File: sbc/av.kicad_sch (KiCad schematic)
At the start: 4 parts, among them J5 AVD-Header, J6 AVA-Header, J7 AudioOut-Connector, J8 VideoOut-Connector

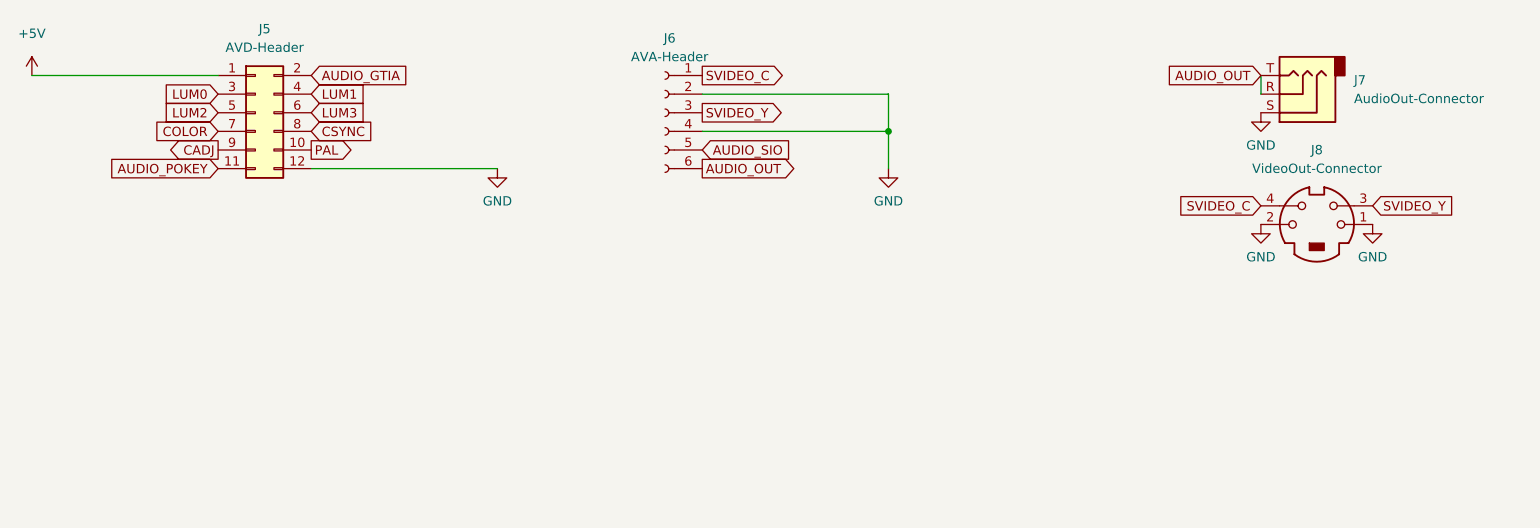
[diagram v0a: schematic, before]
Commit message: SBC v1.1
PCB fixes/changes:

  - Permanently power voltage translators
  - Conservatively specified a slower SRAM (the previous/faster SRAM does actually work fine)
  - RMU: Speculatively provided unbuffered PHI0 input and OE output (not actually needed)
  - Add pullups to open drain GTIA outputs
  - Plot selected values on silk screen
  - Accommodate KiCad 7 upgrade

- PLD changes:
  - Fix AMU logic
  - Fix RMU (unbuffered PHI0 and OE output not needed)

- QTPY firmware:
  - add soft power on/off support (Ctrl-F12)
  - reflects switched power and usb state in the neopixel
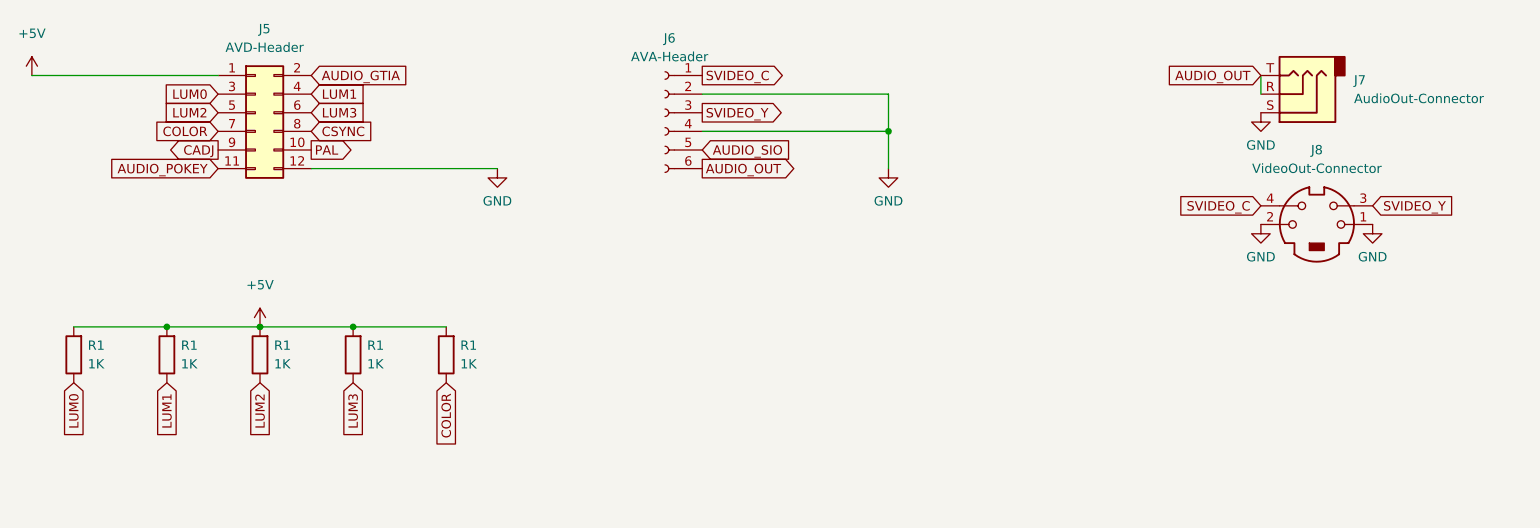
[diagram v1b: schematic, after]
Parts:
- added R1 (x5): 1K, Resistor_SMD:R_0805_2012Metric_Pad1.20x1.40mm_HandSolder, symbol Device:R
- J6: symbol Connector:Conn_01x06_Female -> Connector:Conn_01x06_Socket
- J7: symbol Connector:AudioJack3 -> Connector_Audio:AudioJack3
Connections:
- net +5V: now also R1.2, R1.2, R1.2, R1.2, R1.2
- net COLOR: now also R1.1
- net LUM0: now also R1.1
- net LUM1: now also R1.1
- net LUM2: now also R1.1
- net LUM3: now also R1.1

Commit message: SBC v1.2
SBC fixes/changes:

  - S-Video:
    - Fix S-Video footprint (Y and C swapped, and GNDs swapped) and adapt schematic to match
    - Wire S-Video grounds to AVA header instead of directly to (digital) GND
  - Audio:
    - Wire Audio-Out ground to AVA header
    - Drop SIO audio
    - Pullup open drain pokey audio
  - AMU/RMU:
    - Connect ROM and RAM OE to GND
    - Reserve AMU pin for "IO"
    - Reserve RMU pin for "antic" (registered halt)
    - Support for separate Antic banking (clock RMU with /phi2)
    - Supoprt 130XE and 320XE (compy)
  - Add the option for a resistor between OSC, PHI0 buffer and PHI2 buffer (to reduce over/under-shoot)
  - Invert CA2 (a PNP transistor on the Atari 800 XL inverts this signal)

Additions:

  - SBC Audio/Video board
  - SBC Case
  - SBC SD board

Stylize the complete system as "SFF 320XE".
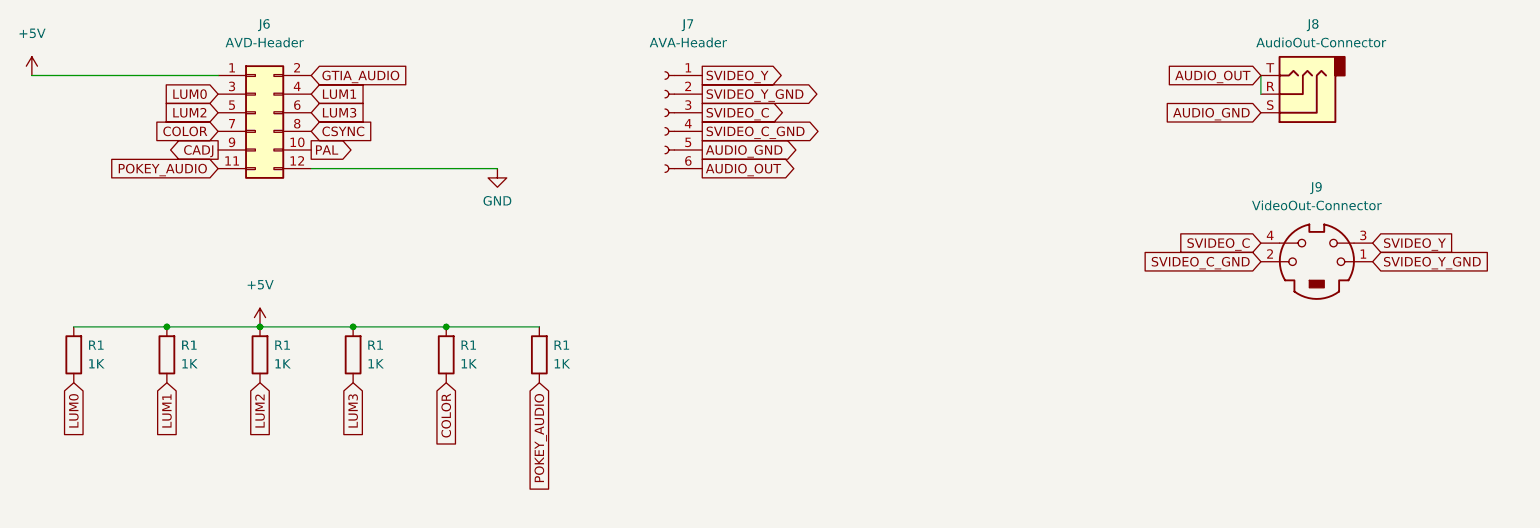
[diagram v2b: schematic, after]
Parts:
- added R1: 1K, Resistor_SMD:R_0805_2012Metric_Pad1.20x1.40mm_HandSolder, symbol Device:R
- renumbered J5 to J6, J6 to J7, J7 to J8, J8 to J9
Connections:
- net +5V: now also R1.2
- net GND: no longer J7.2 (Pin_2), J7.4 (Pin_4), J8.S, J9.1, J9.2
- net SVIDEO_C: now also J7.3 (Pin_3); no longer J7.1 (Pin_1)
- net SVIDEO_Y: now also J7.1 (Pin_1); no longer J7.3 (Pin_3)
- net AUDIO_GTIA renamed GTIA_AUDIO
- net AUDIO_POKEY renamed POKEY_AUDIO
- net POKEY_AUDIO: now also R1.1
- net AUDIO_SIO renamed AUDIO_GND
- net AUDIO_GND: now also J8.S
- new net SVIDEO_C_GND: J7.4 (Pin_4), J9.2
- new net SVIDEO_Y_GND: J7.2 (Pin_2), J9.1
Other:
- moved on the sheet: J9

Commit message: SBC v1.3
Motherboard updates:

  - KiCad 9 upgrade
  - USB-C power connector
  - Replace EOL resistor packs with discrete SMD resistors
  - Power/enable voltage translators from switched 5V
  - Fix motor signal pullup
  - Eliminate loop in phi2 traces
  - Thicker clock signal traces

SD card adapter updates:

  - KiCad 9 upgrade
  - Power/enable voltage translator from switched 5V and the eliminate unnecessary SIO pullups

Audio/Video adapter updates:

  - KiCad 9 upgrade
  - No functional changes, gerbers not regenerated, cleaned up bom
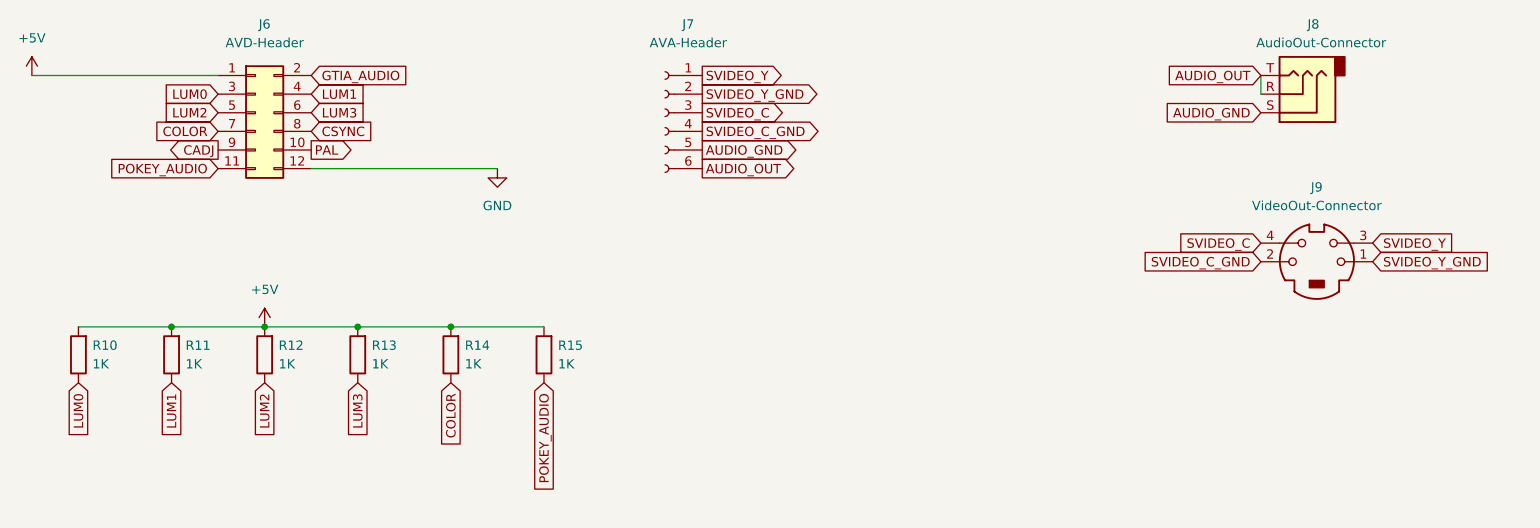
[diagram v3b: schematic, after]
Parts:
- renumbered R1 to R10, R1 to R11, R1 to R12, R1 to R13, R1 to R14, R1 to R15
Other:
- moved on the sheet: R10, R11, R12, R13, R14, R15
